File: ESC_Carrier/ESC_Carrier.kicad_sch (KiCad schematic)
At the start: 21 parts, among them J10 Molex 430450821, J11 Molex 43045-0627, J12 Molex 43045-0627, J13 Molex 43045-0627, J14 Molex 43045-0627, J15 Molex 43045-0627, J16 Molex 43045-0627, J17 Molex 43045-0627, J18 Molex 43045-0627, J9 Molex 53047-0510

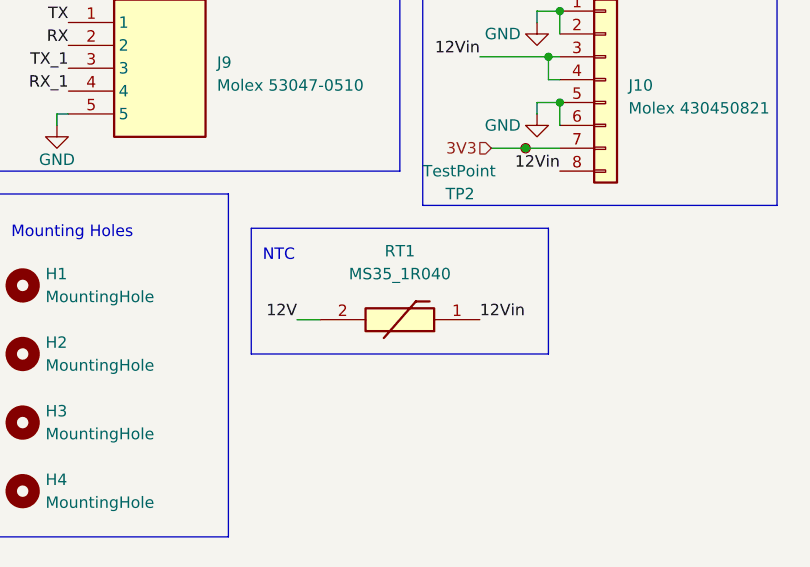
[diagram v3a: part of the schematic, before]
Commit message: Feat: switched thermistor to AS32_1R030, minor fixes
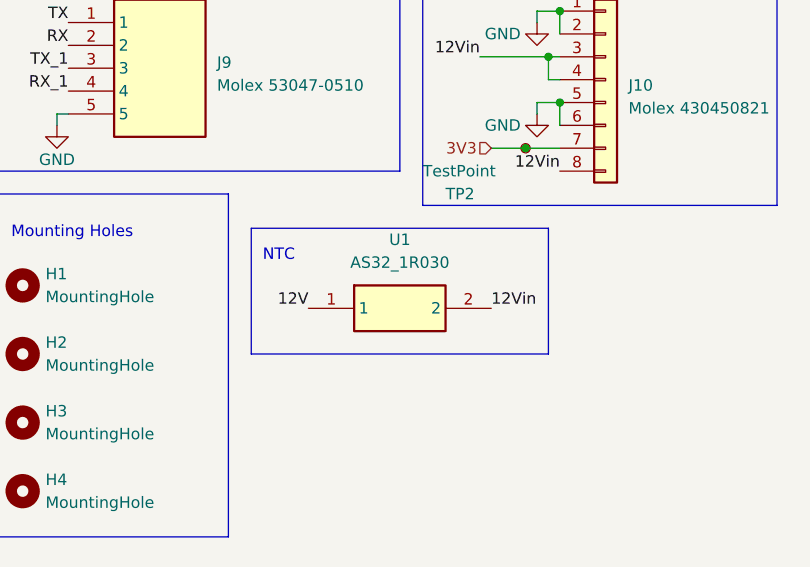
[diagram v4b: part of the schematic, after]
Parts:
- removed RT1: MS35_1R040, MS351R040, symbol MS35_1R040:MS35_1R040
- added U1: AS32_1R030, AS321R030, symbol AS32_1R030:AS32_1R030
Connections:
- net 12V: now also U1.1
- net 12Vin: now also U1.2
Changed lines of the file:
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@@
-    (stroke (width 0) (type default))
-  )
-  (wire (pts (xy 113.03 125.73) (xy 115.57 125.73))
     (stroke (width 0) (type default))
   )
@@
     (effects (font (size 1.27 1.27)) (justify left bottom))
   )
-  (label "12V" (at 113.03 125.73 180) (fields_autoplaced)
+  (label "12V" (at 114.3 124.46 180) (fields_autoplaced)
     (effects (font (size 1.27 1.27)) (justify right bottom))
   )
@@
     (effects (font (size 1.27 1.27)) (justify left bottom))
   )
-  (label "12Vin" (at 133.35 125.73 0) (fields_autoplaced)
+  (label "12Vin" (at 134.62 124.46 0) (fields_autoplaced)
     (effects (font (size 1.27 1.27)) (justify left bottom))
   )
@@
         (path "/bda61329-80a1-4402-a8ce-b974364c2747"
           (reference "#PWR01") (unit 1)
-        )
-      )
-    )
-  )
-  (symbol (lib_id "MS35_1R040:MS35_1R040") (at 133.35 125.73 180) (unit 1)
-    (in_bom yes) (on_board yes) (dnp no) (fields_autoplaced)
-    (property "Reference" "RT1" (at 124.46 118.11 0)
-      (effects (font (size 1.27 1.27)))
-    )
-    (property "Value" "MS35_1R040" (at 124.46 120.65 0)
-      (effects (font (size 1.27 1.27)))
-    )
-    (property "Footprint" "MS351R040" (at 119.38 29.54 0)
-      (effects (font (size 1.27 1.27)) (justify left top) hide)
-    )
-    (property "Datasheet" "" (at 119.38 -70.46 0)
-      (effects (font (size 1.27 1.27)) (justify left top) hide)
-    )
-    (property "Height" "37" (at 119.38 -270.46 0)
-      (effects (font (size 1.27 1.27)) (justify left top) hide)
-    )
-    (property "Mouser Part Number" "995-MS35-1R040" (at 119.38 -370.46 0)
-      (effects (font (size 1.27 1.27)) (justify left top) hide)
-    )
-    (property "Mouser Price/Stock" "https://www.mouser.co.uk/ProductDetail/Ametherm/MS35-1R040?qs=PVyXUKBeRH0GWXbdb%2F8Hsg%3D%3D" (at 119.38 -470.46 0)
-      (effects (font (size 1.27 1.27)) (justify left top) hide)
-    )
-    (property "Manufacturer_Name" "AMETHERM" (at 119.38 -570.46 0)
-      (effects (font (size 1.27 1.27)) (justify left top) hide)
-    )
-    (property "Manufacturer_Part_Number" "MS35 1R040" (at 119.38 -670.46 0)
-      (effects (font (size 1.27 1.27)) (justify left top) hide)
-    )
-    (pin "1")
-    (pin "2")
-    (instances
-      (project "ESC_Carrier"
-        (path "/bda61329-80a1-4402-a8ce-b974364c2747"
-          (reference "RT1") (unit 1)
         )
       )
@@
         )
       )
+    )
+  )
+  (symbol (lib_id "AS32_1R030:AS32_1R030") (at 114.3 124.46 0) (unit 1)
+    (in_bom yes) (on_board yes) (dnp no) (fields_autoplaced)
+    (property "Reference" "U1" (at 124.46 116.84 0)
+      (effects (font (size 1.27 1.27)))
+    )
+    (property "Value" "AS32_1R030" (at 124.46 119.38 0)
+      (effects (font (size 1.27 1.27)))
+    )
+    (property "Footprint" "AS321R030" (at 130.81 219.38 0)
+      (effects (font (size 1.27 1.27)) (justify left top) hide)
+    )
+    (property "Datasheet" "https://www.ametherm.com/datasheets/as321r030.html" (at 130.81 319.38 0)
+      (effects (font (size 1.27 1.27)) (justify left top) hide)
+    )
+    (property "Height" "30" (at 130.81 519.38 0)
+      (effects (font (size 1.27 1.27)) (justify left top) hide)
+    )
+    (property "Manufacturer_Name" "AMETHERM" (at 130.81 619.38 0)
+      (effects (font (size 1.27 1.27)) (justify left top) hide)
+    )
+    (property "Manufacturer_Part_Number" "AS32 1R030" (at 130.81 719.38 0)
+      (effects (font (size 1.27 1.27)) (justify left top) hide)
+    )
+    (property "Mouser Part Number" "995-AS32-1R030" (at 130.81 819.38 0)
+      (effects (font (size 1.27 1.27)) (justify left top) hide)
+    )
+    (property "Mouser Price/Stock" "https://www.mouser.co.uk/ProductDetail/Ametherm/AS32-1R030?qs=PVyXUKBeRH36hEJbGSKXOw%3D%3D" (at 130.81 919.38 0)
+      (effects (font (size 1.27 1.27)) (justify left top) hide)
+    )
+    (property "Arrow Part Number" "" (at 130.81 1019.38 0)
+      (effects (font (size 1.27 1.27)) (justify left top) hide)
+    )
+    (property "Arrow Price/Stock" "" (at 130.81 1119.38 0)
+      (effects (font (size 1.27 1.27)) (justify left top) hide)
+    )
+    (pin "1")
+    (pin "2")
+    (instances
+      (project "ESC_Carrier"
+        (path "/bda61329-80a1-4402-a8ce-b974364c2747"
+          (reference "U1") (unit 1)
+        )
+      )

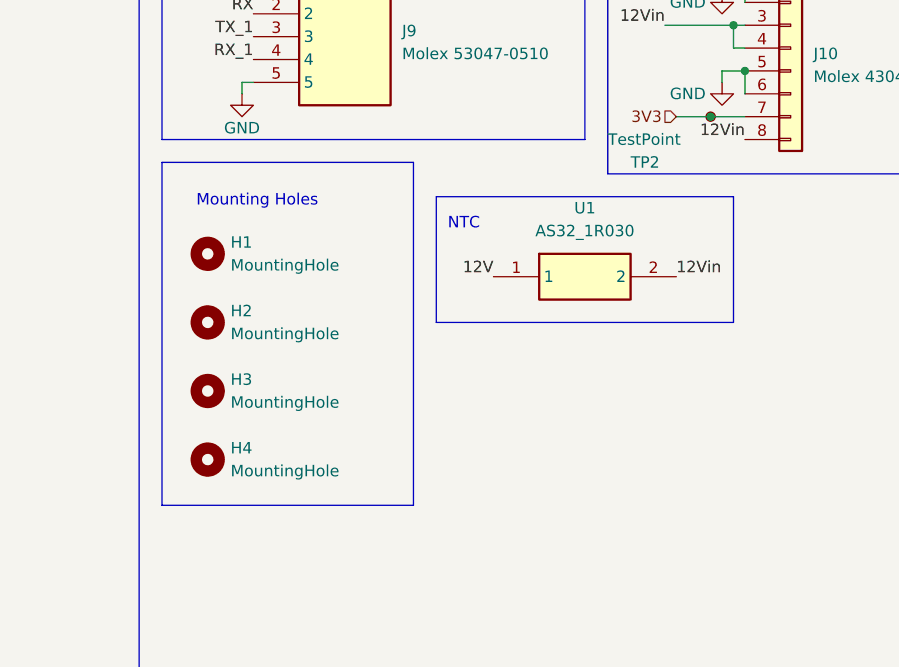
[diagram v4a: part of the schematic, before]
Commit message: Feat: added 12v zone, reduced size, switched mounting hole format
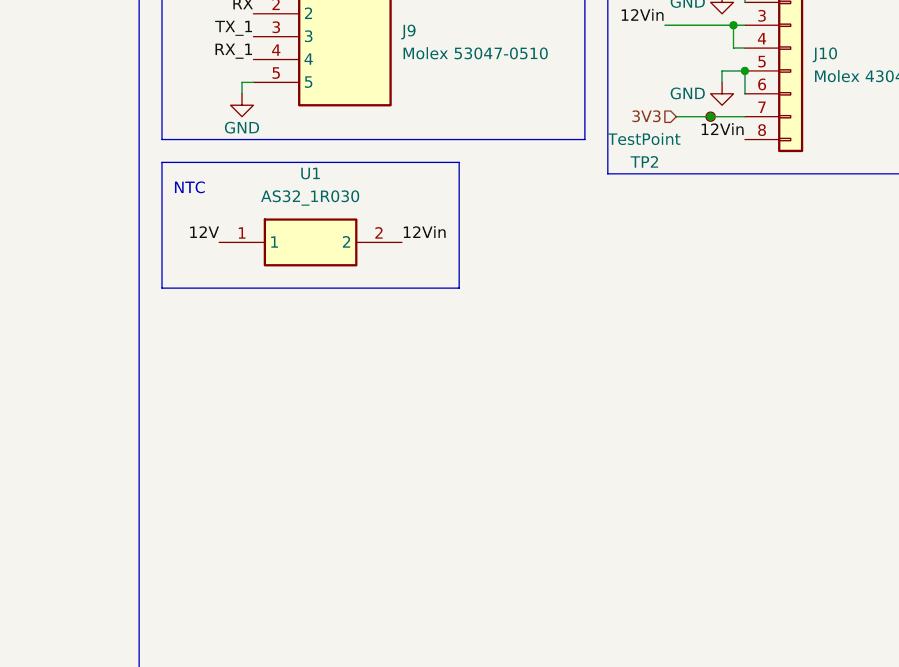
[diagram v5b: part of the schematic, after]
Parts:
- removed H1, H2, H3, H4: MountingHole, MountingHole:MountingHole_2.7mm_M2.5, symbol Mechanical:MountingHole
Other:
- note removed: "Mounting Holes"
- moved on the sheet: U1
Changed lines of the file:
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@@
     (stroke (width 0) (type default))
-  )
-  (rectangle (start 77.47 111.76) (end 105.41 149.86)
-    (stroke (width 0) (type default))
-    (fill (type none))
   )
   (rectangle (start 77.47 12.7) (end 180.34 81.28)
@@
     (fill (type none))
   )
-  (rectangle (start 107.95 115.57) (end 140.97 129.54)
+  (rectangle (start 77.47 111.76) (end 110.49 125.73)
     (stroke (width 0) (type default))
     (fill (type none))
@@
   )
   (text "NTC" (exclude_from_sim no)
- (at 109.22 119.38 0)
+ (at 78.74 115.57 0)
     (effects (font (size 1.27 1.27)) (justify left bottom))
   )
@@
     (effects (font (size 1.27 1.27)) (justify right bottom))
   )
-  (text "Mounting Holes" (exclude_from_sim no)
- (at 81.28 116.84 0)
-    (effects (font (size 1.27 1.27)) (justify left bottom))
-  )
   (text "ESC Carrier to Power" (exclude_from_sim no)
  (at 156.21 87.63 0)
@@
     (effects (font (size 1.27 1.27)) (justify left bottom))
   )
-  (label "12V" (at 114.3 124.46 180) (fields_autoplaced)
+  (label "12V" (at 83.82 120.65 180) (fields_autoplaced)
     (effects (font (size 1.27 1.27)) (justify right bottom))
   )
@@
     (effects (font (size 1.27 1.27)) (justify left bottom))
   )
-  (label "12Vin" (at 134.62 124.46 0) (fields_autoplaced)
+  (label "12Vin" (at 104.14 120.65 0) (fields_autoplaced)
     (effects (font (size 1.27 1.27)) (justify left bottom))
   )
@@
     )
   )
-  (symbol (lib_id "Mechanical:MountingHole") (at 82.55 144.78 0) (unit 1)
-    (in_bom yes) (on_board yes) (dnp no) (fields_autoplaced)
-    (property "Reference" "H4" (at 85.09 143.51 0)
-      (effects (font (size 1.27 1.27)) (justify left))
-    )
-    (property "Value" "MountingHole" (at 85.09 146.05 0)
-      (effects (font (size 1.27 1.27)) (justify left))
-    )
-    (property "Footprint" "MountingHole:MountingHole_2.7mm_M2.5" (at 82.55 144.78 0)
-      (effects (font (size 1.27 1.27)) hide)
-    )
-    (property "Datasheet" "~" (at 82.55 144.78 0)
-      (effects (font (size 1.27 1.27)) hide)
-    )
-    (instances
-      (project "ESC_Carrier"
-        (path "/bda61329-80a1-4402-a8ce-b974364c2747"
-          (reference "H4") (unit 1)
-        )
-      )
-    )
-  )
   (symbol (lib_id "43045-0627:43045-0627") (at 91.44 40.64 0) (unit 1)
     (in_bom yes) (on_board yes) (dnp no) (fields_autoplaced)
@@
     )
   )
-  (symbol (lib_id "AS32_1R030:AS32_1R030") (at 114.3 124.46 0) (unit 1)
+  (symbol (lib_id "AS32_1R030:AS32_1R030") (at 83.82 120.65 0) (unit 1)
     (in_bom yes) (on_board yes) (dnp no) (fields_autoplaced)
-    (property "Reference" "U1" (at 124.46 116.84 0)
-      (effects (font (size 1.27 1.27)))
-    )
-    (property "Value" "AS32_1R030" (at 124.46 119.38 0)
-      (effects (font (size 1.27 1.27)))
-    )
-    (property "Footprint" "AS321R030" (at 130.81 219.38 0)
-      (effects (font (size 1.27 1.27)) (justify left top) hide)
-    )
-    (property "Datasheet" "https://www.ametherm.com/datasheets/as321r030.html" (at 130.81 319.38 0)
-      (effects (font (size 1.27 1.27)) (justify left top) hide)
-    )
-    (property "Height" "30" (at 130.81 519.38 0)
-      (effects (font (size 1.27 1.27)) (justify left top) hide)
-    )
-    (property "Manufacturer_Name" "AMETHERM" (at 130.81 619.38 0)
-      (effects (font (size 1.27 1.27)) (justify left top) hide)
-    )
-    (property "Manufacturer_Part_Number" "AS32 1R030" (at 130.81 719.38 0)
-      (effects (font (size 1.27 1.27)) (justify left top) hide)
-    )
-    (property "Mouser Part Number" "995-AS32-1R030" (at 130.81 819.38 0)
-      (effects (font (size 1.27 1.27)) (justify left top) hide)
-    )
-    (property "Mouser Price/Stock" "https://www.mouser.co.uk/ProductDetail/Ametherm/AS32-1R030?qs=PVyXUKBeRH36hEJbGSKXOw%3D%3D" (at 130.81 919.38 0)
-      (effects (font (size 1.27 1.27)) (justify left top) hide)
-    )
-    (property "Arrow Part Number" "" (at 130.81 1019.38 0)
-      (effects (font (size 1.27 1.27)) (justify left top) hide)
-    )
-    (property "Arrow Price/Stock" "" (at 130.81 1119.38 0)
+    (property "Reference" "U1" (at 93.98 113.03 0)
+      (effects (font (size 1.27 1.27)))
+    )
+    (property "Value" "AS32_1R030" (at 93.98 115.57 0)
+      (effects (font (size 1.27 1.27)))
+    )
+    (property "Footprint" "AS321R030" (at 100.33 215.57 0)
+      (effects (font (size 1.27 1.27)) (justify left top) hide)
+    )
+    (property "Datasheet" "https://www.ametherm.com/datasheets/as321r030.html" (at 100.33 315.57 0)
+      (effects (font (size 1.27 1.27)) (justify left top) hide)
+    )
+    (property "Height" "30" (at 100.33 515.57 0)
+      (effects (font (size 1.27 1.27)) (justify left top) hide)
+    )
+    (property "Manufacturer_Name" "AMETHERM" (at 100.33 615.57 0)
+      (effects (font (size 1.27 1.27)) (justify left top) hide)
+    )
+    (property "Manufacturer_Part_Number" "AS32 1R030" (at 100.33 715.57 0)
+      (effects (font (size 1.27 1.27)) (justify left top) hide)
+    )
+    (property "Mouser Part Number" "995-AS32-1R030" (at 100.33 815.57 0)
+      (effects (font (size 1.27 1.27)) (justify left top) hide)
+    )
+    (property "Mouser Price/Stock" "https://www.mouser.co.uk/ProductDetail/Ametherm/AS32-1R030?qs=PVyXUKBeRH36hEJbGSKXOw%3D%3D" (at 100.33 915.57 0)
+      (effects (font (size 1.27 1.27)) (justify left top) hide)
+    )
+    (property "Arrow Part Number" "" (at 100.33 1015.57 0)
+      (effects (font (size 1.27 1.27)) (justify left top) hide)
+    )
+    (property "Arrow Price/Stock" "" (at 100.33 1115.57 0)
       (effects (font (size 1.27 1.27)) (justify left top) hide)
     )
@@
     )
   )
-  (symbol (lib_id "Mechanical:MountingHole") (at 82.55 137.16 0) (unit 1)
-    (in_bom yes) (on_board yes) (dnp no) (fields_autoplaced)
-    (property "Reference" "H3" (at 85.09 135.89 0)
-      (effects (font (size 1.27 1.27)) (justify left))
-    )
-    (property "Value" "MountingHole" (at 85.09 138.43 0)
-      (effects (font (size 1.27 1.27)) (justify left))
-    )
-    (property "Footprint" "MountingHole:MountingHole_2.7mm_M2.5" (at 82.55 137.16 0)
-      (effects (font (size 1.27 1.27)) hide)
-    )
-    (property "Datasheet" "~" (at 82.55 137.16 0)
-      (effects (font (size 1.27 1.27)) hide)
-    )
-    (instances
-      (project "ESC_Carrier"
-        (path "/bda61329-80a1-4402-a8ce-b974364c2747"
-          (reference "H3") (unit 1)
-        )
-      )
-    )
-  )
   (symbol (lib_id "Connector:TestPoint_Small") (at 20.32 25.4 0) (unit 1)
     (in_bom yes) (on_board yes) (dnp no)
@@
         )
       )
-    )
-  )
-  (symbol (lib_id "Mechanical:MountingHole") (at 82.55 129.54 0) (unit 1)
-    (in_bom yes) (on_board yes) (dnp no) (fields_autoplaced)
-    (property "Reference" "H2" (at 85.09 128.27 0)
-      (effects (font (size 1.27 1.27)) (justify left))
-    )
-    (property "Value" "MountingHole" (at 85.09 130.81 0)
-      (effects (font (size 1.27 1.27)) (justify left))
-    )
-    (property "Footprint" "MountingHole:MountingHole_2.7mm_M2.5" (at 82.55 129.54 0)
-      (effects (font (size 1.27 1.27)) hide)
-    )
-    (property "Datasheet" "~" (at 82.55 129.54 0)
-      (effects (font (size 1.27 1.27)) hide)
-    )
-    (instances
-      (project "ESC_Carrier"
-        (path "/bda61329-80a1-4402-a8ce-b974364c2747"
-          (reference "H2") (unit 1)
-        )
-      )
-    )
-  )
-  (symbol (lib_id "Mechanical:MountingHole") (at 82.55 121.92 0) (unit 1)
-    (in_bom yes) (on_board yes) (dnp no) (fields_autoplaced)
-    (property "Reference" "H1" (at 85.09 120.65 0)
-      (effects (font (size 1.27 1.27)) (justify left))
-    )
-    (property "Value" "MountingHole" (at 85.09 123.19 0)
-      (effects (font (size 1.27 1.27)) (justify left))
-    )
-    (property "Footprint" "MountingHole:MountingHole_2.7mm_M2.5" (at 82.55 121.92 0)
-      (effects (font (size 1.27 1.27)) hide)
-    )
-    (property "Datasheet" "~" (at 82.55 121.92 0)
-      (effects (font (size 1.27 1.27)) hide)
-    )
-    (instances
-      (project "ESC_Carrier"
-        (path "/bda61329-80a1-4402-a8ce-b974364c2747"
-          (reference "H1") (unit 1)
-        )
-      )

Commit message: Feat: added 3d models
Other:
- title: (none) -> MUREX ESC Carrier Board
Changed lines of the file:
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@@
 (kicad_sch (version 20230409) (generator eeschema)
   (paper "A4")
+  (title_block
+    (title "MUREX ESC Carrier Board")
+    (date "2023-07-20")
+    (rev "V1.0")
+    (comment 1 "MUREX Robotics [Celine Zhang]")
+    (comment 2 "//DREAM BIG. DREAM MUREX.")
+    (comment 3 "in the event of a speed controller failure.")
+    (comment 4 "The MUREX ESC Carrier board is designed for rapid replacement of components")
+  )
   (junction (at 142.24 101.6) (diameter 0) (color 0 0 0 0)
   )

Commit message: Feat[esc_carrier v2.0]: v2.0 production ready
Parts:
- removed J17, J18: Molex 43045-0627, 430450627:43045-06YY_272829, symbol 43045-0627:43045-0627
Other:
- removed sheet TE 5530843-7 7
- removed sheet TE 5530843-7 8
- company: (none) -> MUREX Robotics [Celine Zhang]
- moved on the sheet: J11, J12, J13, J14, J15, J16
